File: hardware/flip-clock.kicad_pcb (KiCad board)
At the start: 2 copper layers, 64.6 x 53.3 mm, 13 parts, among them J1 Screw_Terminal_01x02, J2 Conn_01x04, U1 WeMos_D1_mini

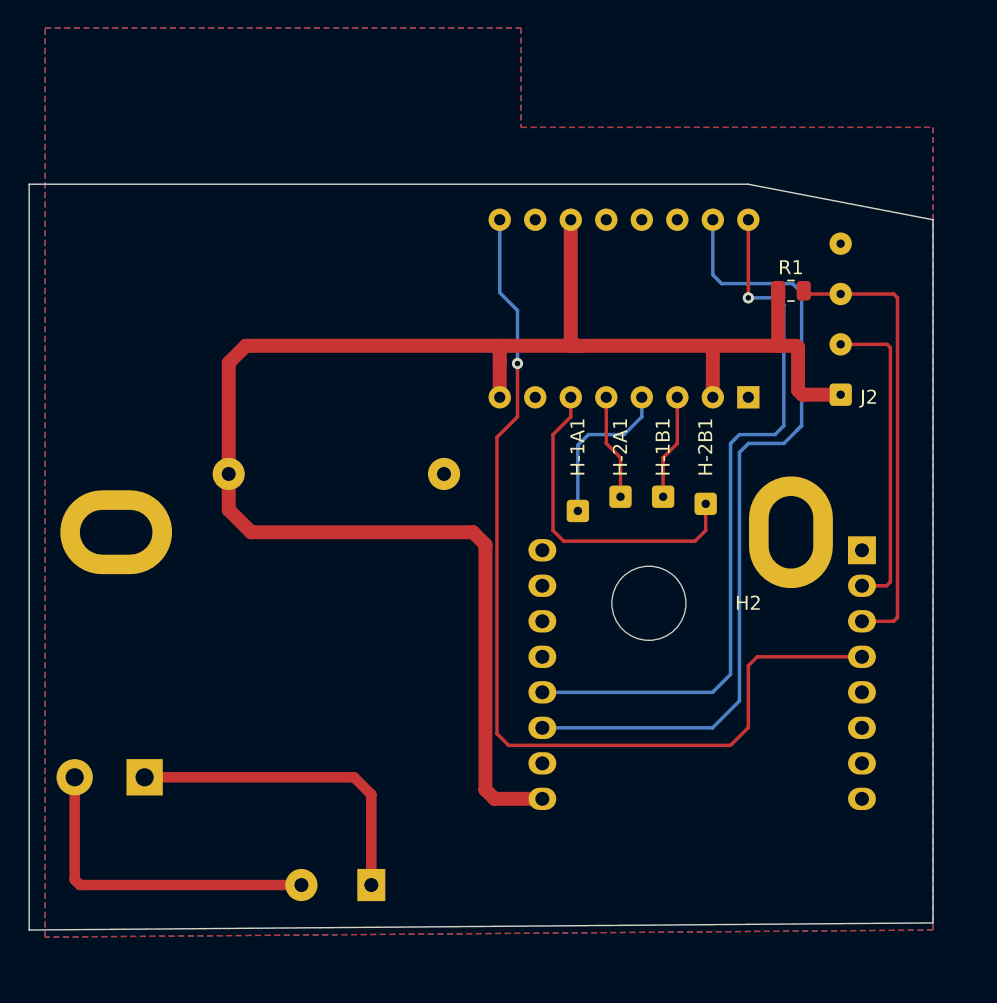
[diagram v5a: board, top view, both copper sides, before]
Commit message: Redesign after fitting probe
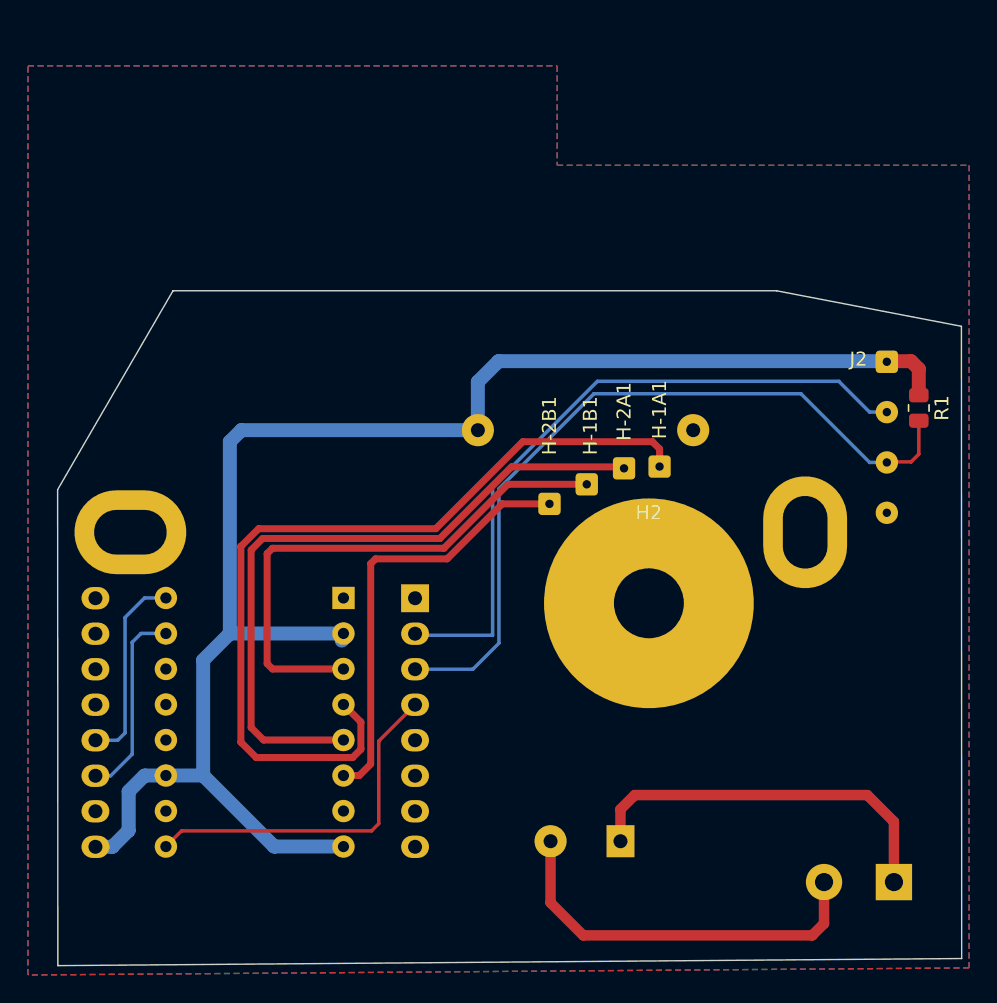
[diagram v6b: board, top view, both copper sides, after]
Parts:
- moved J1 54.1 mm to (175.5, 80.9)
- moved A1 32.3 mm to (136.1, 60.6), turned to 180 degrees
- moved U1 32.1 mm to (141.3, 60.6)
- moved PS1 18.1 mm to (156.0, 78.0)
- moved R1 12.4 mm to (177.3, 47.0), turned to -90 degrees
- moved H-2B1 11.2 mm to (150.9, 53.8), turned to 0 degrees
- moved H-1A1 6.70 mm to (158.9, 51.3), turned to 0 degrees
- moved H-1B1 5.53 mm to (153.5, 52.5), turned to 0 degrees
- moved J2 4.05 mm to (175.0, 43.7), turned to -90 degrees
- moved H-2A1 2.05 mm to (156.2, 51.3), turned to 0 degrees
- moved H1 1.02 mm to (120.9, 55.9)
- moved H3 1.02 mm to (169.2, 55.9)
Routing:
- net /1A: track 11.5 -> 61.6 mm
- net /STEP: track 58.7 -> 13.9 mm
- net //ENABLE: track 69.6 -> 25.5 mm, vias 1 -> 0
- net /2A: track 7.53 -> 48.9 mm
- net /DIR: track 51.8 -> 14.1 mm, vias 1 -> 0
- net /1B: track 7.53 -> 38.4 mm
- net /PD_IN: track 22.6 -> 48.5 mm
- net /HOUR: track 32.4 -> 55.3 mm
- net /2B: track 23.5 -> 31.2 mm
- net VCC: track 120.2 -> 112.8 mm
- net /AC1: track 23.7 -> 28.2 mm
- net /AC2: track 23.2 -> 27.4 mm
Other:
- board size 64.6 x 53.3 mm -> 64.7 x 48.3 mm

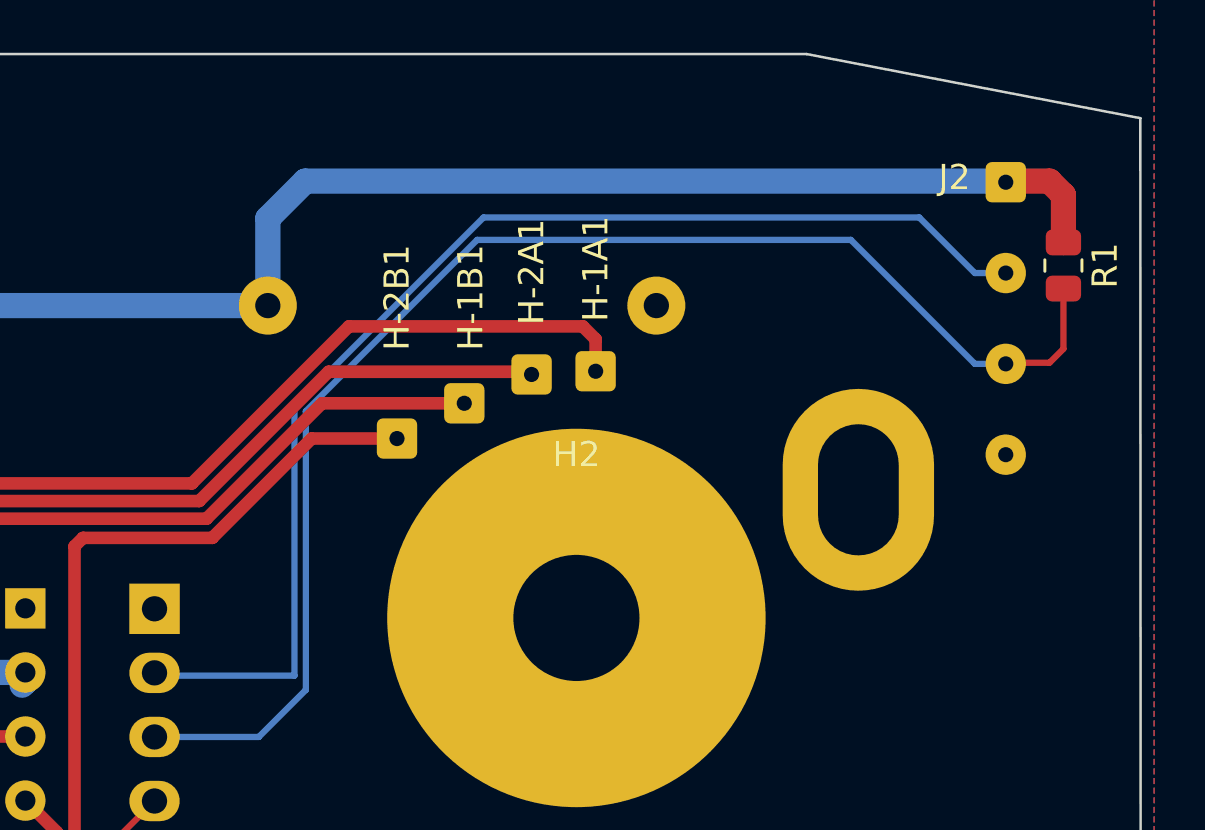
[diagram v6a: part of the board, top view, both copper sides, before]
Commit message: JST Connector for IR and hour
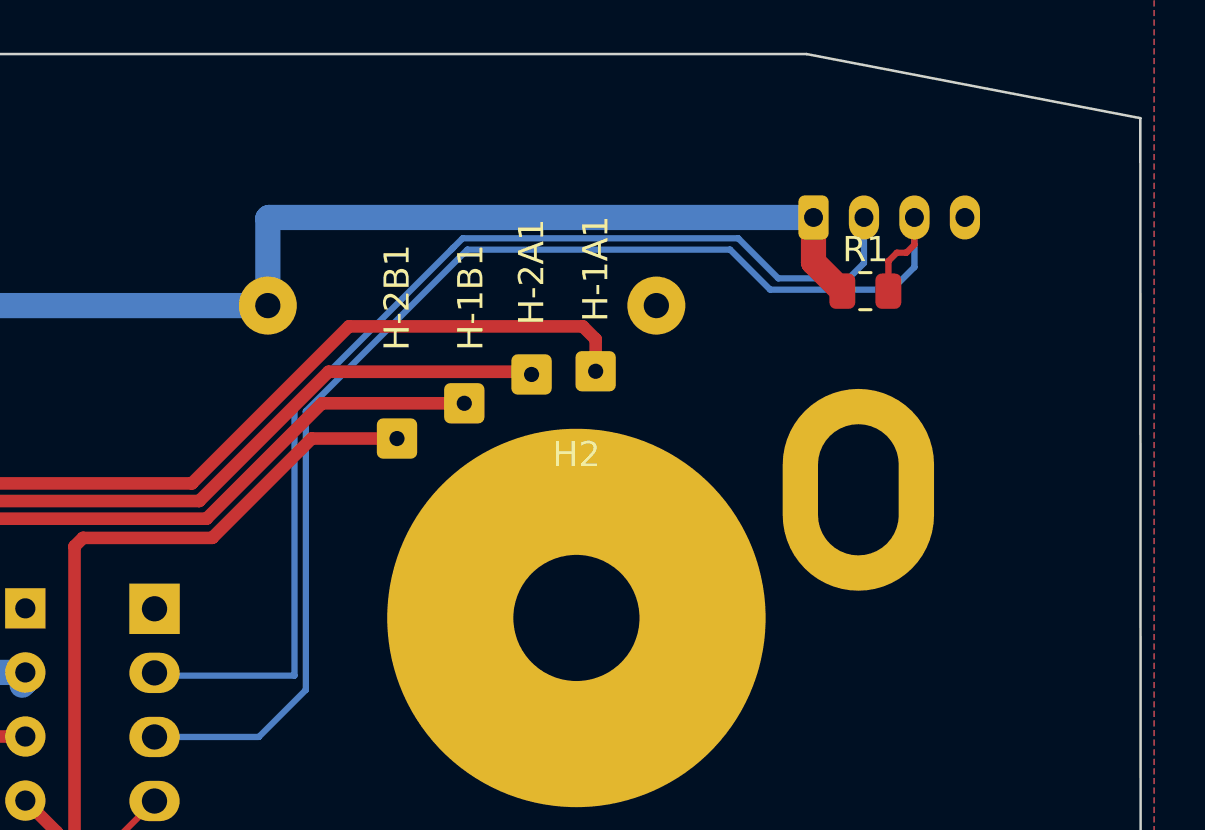
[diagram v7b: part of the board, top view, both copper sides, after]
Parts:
- J2: footprint Connector_Wire:SolderWire-0.1sqmm_1x04_P3.6mm_D0.4mm_OD1mm -> Connector_JST:JST_PH_B4B-PH-K_1x04_P2.00mm_Vertical; moved to B.Cu
- moved R1 7.92 mm to (169.4, 48.0), turned to 0 degrees
- moved J2 7.75 mm to (167.4, 45.1), turned to 0 degrees
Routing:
- net VCC: track 112.8 -> 103.5 mm
- net /HOUR: track 55.3 -> 51.2 mm
- net /PD_IN: track 48.5 -> 44.4 mm

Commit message: second PCB-Part for IR
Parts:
- added H4: MountingHole_Pad, Connector_Wire:SolderWirePad_1x01_SMD_1x2mm, F.Cu at (105.4, 69.8)
- added H5: MountingHole_Pad, Connector_Wire:SolderWirePad_1x01_SMD_1x2mm, F.Cu at (101.6, 69.8)
- added H6: MountingHole_Pad, Connector_Wire:SolderWirePad_1x01_SMD_1x2mm, F.Cu at (109.2, 69.8)
- added Q1: TCRT5000, KiCad:TCRT5000, F.Cu at (105.4, 81.3)
- added R2: 330, Resistor_SMD:R_0805_2012Metric, F.Cu at (108.0, 74.9)
- added R3: 10k, Resistor_SMD:R_0805_2012Metric, F.Cu at (100.3, 74.9)
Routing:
- net /Sense: track 0.00 -> 14.1 mm
- net /+: track 0.00 -> 10.9 mm
- net Net-(Q1-Pad4): track 0.00 -> 5.37 mm
- net (no net): vias 0 -> 8
- added copper zone on F.Cu, net /-
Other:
- board size 64.7 x 48.3 mm -> 82.5 x 47.8 mm
- board text added: "+"
- board text added: "-"
- board text added: "S"
